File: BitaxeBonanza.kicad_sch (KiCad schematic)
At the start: 10 parts, among them J1 XT30

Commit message: most placement and routing done
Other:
- sheet Data ports: added 12V; removed none
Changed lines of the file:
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@@
+		(color 0 0 0 0)
+	)
+	(junction
+		(at 78.74 44.45)
+		(diameter 0)
 		(color 0 0 0 0)
 	)
@@
 	(wire
 		(pts
-			(xy 58.42 44.45) (xy 102.87 44.45)
+			(xy 58.42 44.45) (xy 78.74 44.45)
 		)
 		(stroke
@@
 	(wire
 		(pts
-			(xy 90.17 125.73) (xy 102.87 125.73)
+			(xy 90.17 129.54) (xy 102.87 129.54)
 		)
 		(stroke
@@
 	(wire
 		(pts
+			(xy 102.87 124.46) (xy 78.74 124.46)
+		)
+		(stroke
+			(width 0)
+			(type default)
+		)
+	)
+	(wire
+		(pts
 			(xy 58.42 48.26) (xy 62.23 48.26)
 		)
@@
 	(wire
 		(pts
+			(xy 78.74 44.45) (xy 102.87 44.45)
+		)
+		(stroke
+			(width 0)
+			(type default)
+		)
+	)
+	(wire
+		(pts
 			(xy 86.36 116.84) (xy 102.87 116.84)
 		)
@@
 		(pts
 			(xy 91.44 66.04) (xy 102.87 66.04)
+		)
+		(stroke
+			(width 0)
+			(type default)
+		)
+	)
+	(wire
+		(pts
+			(xy 78.74 124.46) (xy 78.74 44.45)
 		)
 		(stroke
@@
 	)
 	(label "5V_SWITCH"
-		(at 90.17 125.73 0)
+		(at 90.17 129.54 0)
 		(effects
 			(font
@@
 		)
 		(pin "5V_SWITCH" output
-			(at 102.87 125.73 180)
+			(at 102.87 129.54 180)
 			(effects
 				(font
@@
 			)
 		)
+		(pin "12V" input
+			(at 102.87 124.46 180)
+			(effects
+				(font
+					(size 1.27 1.27)
+				)
+				(justify left)
+			)
+		)

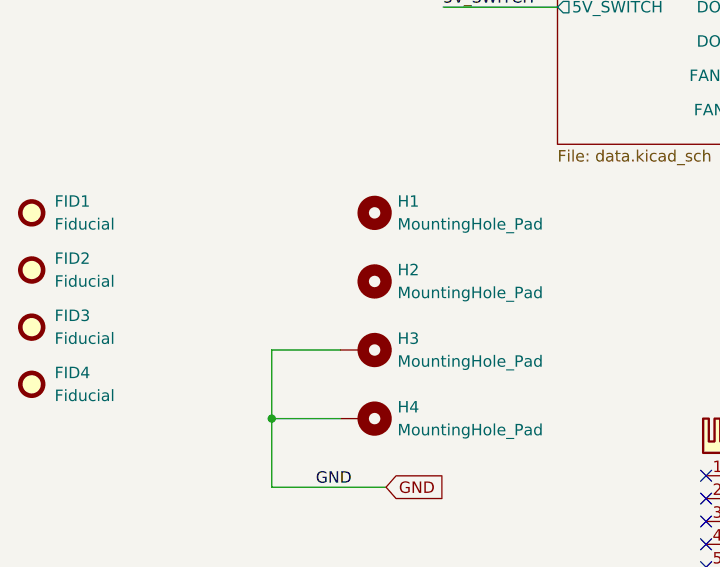
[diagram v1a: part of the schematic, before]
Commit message: changed TPS82130 voltage regulators to TPSM82903. Connected ESP32<->RP2040 CTRL serial port. made top mounting holes plated.
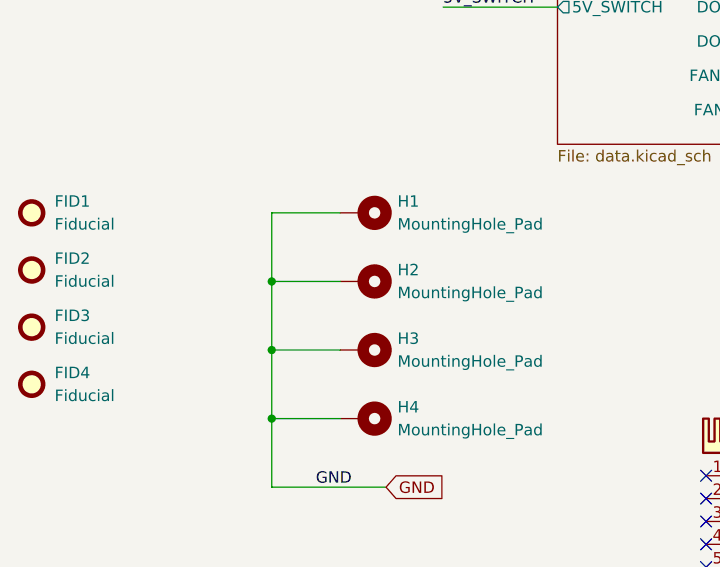
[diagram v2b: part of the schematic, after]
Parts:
- H1, H2: footprint MountingHole:MountingHole_3.2mm_M3 -> MountingHole:MountingHole_3.2mm_M3_Pad_Via; symbol Mechanical:MountingHole -> Mechanical:MountingHole_Pad
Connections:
- net GND: now also H1.1, H2.1
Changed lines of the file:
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@@
+	)
+	(junction
+		(at 71.12 160.02)
+		(diameter 0)
+		(color 0 0 0 0)
 	)
 	(junction
@@
 		(color 0 0 0 0)
 	)
+	(junction
+		(at 71.12 167.64)
+		(diameter 0)
+		(color 0 0 0 0)
+	)
 	(no_connect
 		(at 119.38 189.23)
@@
 	(wire
 		(pts
+			(xy 71.12 160.02) (xy 78.74 160.02)
+		)
+		(stroke
+			(width 0)
+			(type default)
+		)
+	)
+	(wire
+		(pts
 			(xy 153.67 116.84) (xy 128.27 116.84)
 		)
@@
 	(wire
 		(pts
+			(xy 78.74 152.4) (xy 71.12 152.4)
+		)
+		(stroke
+			(width 0)
+			(type default)
+		)
+	)
+	(wire
+		(pts
 			(xy 151.13 57.15) (xy 151.13 113.03)
 		)
@@
 	(wire
 		(pts
+			(xy 71.12 152.4) (xy 71.12 160.02)
+		)
+		(stroke
+			(width 0)
+			(type default)
+		)
+	)
+	(wire
+		(pts
 			(xy 148.59 53.34) (xy 148.59 109.22)
 		)
@@
 		(pts
 			(xy 128.27 140.97) (xy 198.12 140.97)
+		)
+		(stroke
+			(width 0)
+			(type default)
+		)
+	)
+	(wire
+		(pts
+			(xy 71.12 160.02) (xy 71.12 167.64)
 		)
 		(stroke
@@
 	)
 	(symbol
-		(lib_id "Mechanical:MountingHole")
-		(at 82.55 160.02 270)
+		(lib_id "Mechanical:MountingHole_Pad")
+		(at 81.28 160.02 270)
 		(unit 1)
 		(exclude_from_sim no)
@@
 			)
 		)
-		(property "Footprint" "MountingHole:MountingHole_3.2mm_M3"
-			(at 82.55 160.02 0)
+		(property "Footprint" "MountingHole:MountingHole_3.2mm_M3_Pad_Via"
+			(at 81.28 160.02 0)
 			(effects
 				(font
@@
 		)
 		(property "Datasheet" "~"
-			(at 82.55 160.02 0)
-			(effects
-				(font
-					(size 1.27 1.27)
-				)
-				(hide yes)
-			)
-		)
-		(property "Description" "Mounting Hole without connection"
-			(at 82.55 160.02 0)
+			(at 81.28 160.02 0)
+			(effects
+				(font
+					(size 1.27 1.27)
+				)
+				(hide yes)
+			)
+		)
+		(property "Description" "Mounting Hole with connection"
+			(at 81.28 160.02 0)
 			(effects
 				(font
@@
 		)
 		(property "Mouser" ""
-			(at 82.55 160.02 90)
+			(at 81.28 160.02 90)
 			(effects
 				(font
@@
 		)
 		(property "Manufacturer" ""
-			(at 82.55 160.02 90)
-			(effects
-				(font
-					(size 1.27 1.27)
-				)
-				(hide yes)
-			)
+			(at 81.28 160.02 90)
+			(effects
+				(font
+					(size 1.27 1.27)
+				)
+				(hide yes)
+			)
+		)
+		(pin "1"
 		)
 		(instances
@@
 	)
 	(symbol
-		(lib_id "Mechanical:MountingHole")
-		(at 82.55 152.4 270)
+		(lib_id "Mechanical:MountingHole_Pad")
+		(at 81.28 152.4 270)
 		(unit 1)
 		(exclude_from_sim no)
@@
 			)
 		)
-		(property "Footprint" "MountingHole:MountingHole_3.2mm_M3"
-			(at 82.55 152.4 0)
+		(property "Footprint" "MountingHole:MountingHole_3.2mm_M3_Pad_Via"
+			(at 81.28 152.4 0)
 			(effects
 				(font
@@
 		)
 		(property "Datasheet" "~"
-			(at 82.55 152.4 0)
-			(effects
-				(font
-					(size 1.27 1.27)
-				)
-				(hide yes)
-			)
-		)
-		(property "Description" "Mounting Hole without connection"
-			(at 82.55 152.4 0)
+			(at 81.28 152.4 0)
+			(effects
+				(font
+					(size 1.27 1.27)
+				)
+				(hide yes)
+			)
+		)
+		(property "Description" "Mounting Hole with connection"
+			(at 81.28 152.4 0)
 			(effects
 				(font
@@
 		)
 		(property "Mouser" ""
-			(at 82.55 152.4 90)
+			(at 81.28 152.4 90)
 			(effects
 				(font
@@
 		)
 		(property "Manufacturer" ""
-			(at 82.55 152.4 90)
-			(effects
-				(font
-					(size 1.27 1.27)
-				)
-				(hide yes)
-			)
+			(at 81.28 152.4 90)
+			(effects
+				(font
+					(size 1.27 1.27)
+				)
+				(hide yes)
+			)
+		)
+		(pin "1"
 		)
 		(instances

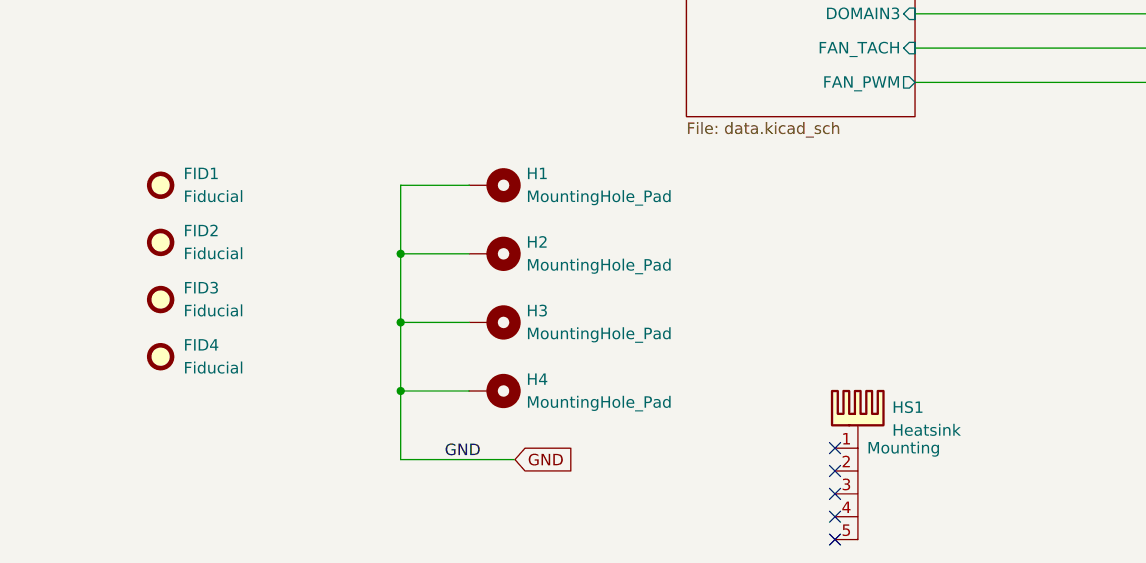
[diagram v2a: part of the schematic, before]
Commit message: switched to SMD FFC for the display connector
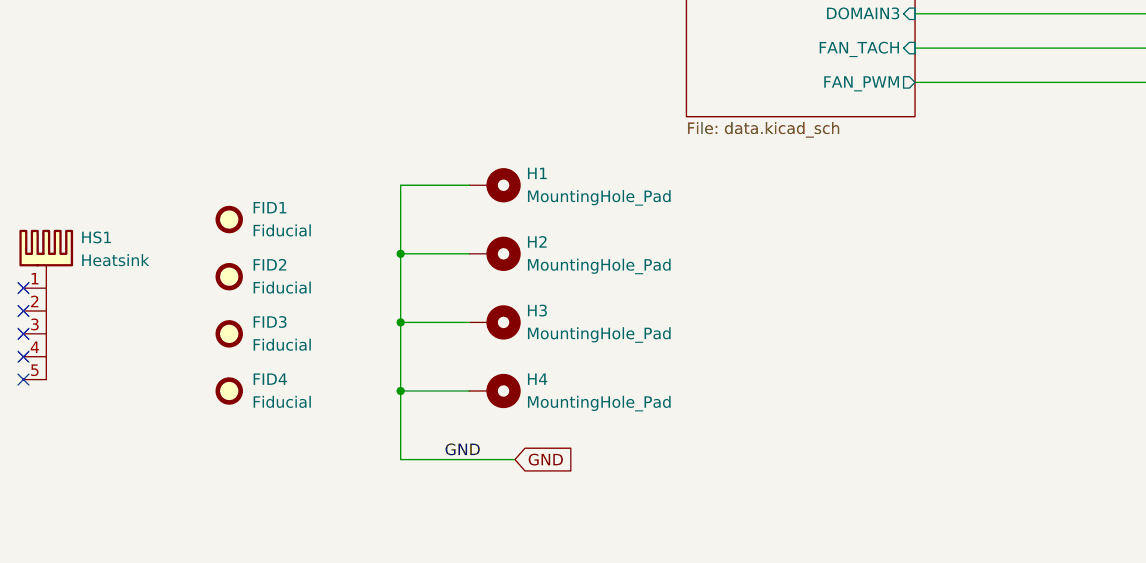
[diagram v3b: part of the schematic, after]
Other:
- moved on the sheet: FID1, FID2, FID3, FID4
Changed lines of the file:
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@@
 	)
 	(no_connect
-		(at 119.38 189.23)
+		(at 29.21 171.45)
 	)
 	(no_connect
-		(at 119.38 186.69)
+		(at 29.21 168.91)
 	)
 	(no_connect
-		(at 119.38 191.77)
+		(at 29.21 173.99)
 	)
 	(no_connect
-		(at 119.38 181.61)
+		(at 29.21 163.83)
 	)
 	(no_connect
-		(at 119.38 184.15)
+		(at 29.21 166.37)
 	)
 	(wire
@@
 	(symbol
 		(lib_id "bitaxe:Heatsink")
-		(at 121.92 179.07 0)
+		(at 31.75 161.29 0)
 		(unit 1)
 		(exclude_from_sim yes)
@@
 		(on_board yes)
 		(dnp no)
-		(fields_autoplaced yes)
 		(property "Reference" "HS1"
-			(at 125.73 177.1014 0)
+			(at 35.56 158.242 0)
 			(effects
 				(font
@@
 		)
 		(property "Value" "Heatsink"
-			(at 125.73 179.6414 0)
+			(at 35.56 160.782 0)
 			(effects
 				(font
@@
 		)
 		(property "Footprint" "bitaxe:Heatsink-5hole-BitaxeGT"
-			(at 122.2248 179.07 0)
+			(at 32.0548 161.29 0)
 			(effects
 				(font
@@
 		)
 		(property "Datasheet" "~"
-			(at 122.2248 179.07 0)
+			(at 32.0548 161.29 0)
 			(effects
 				(font
@@
 		)
 		(property "Description" "Heatsink"
-			(at 121.92 179.07 0)
+			(at 31.75 161.29 0)
 			(effects
 				(font
@@
 		)
 		(property "Mouser" ""
-			(at 121.92 179.07 0)
+			(at 31.75 161.29 0)
 			(effects
 				(font
@@
 		)
 		(property "Manufacturer" ""
-			(at 121.92 179.07 0)
+			(at 31.75 161.29 0)
 			(effects
 				(font
@@
 	(symbol
 		(lib_id "Mechanical:Fiducial")
-		(at 44.45 158.75 0)
+		(at 52.07 162.56 0)
 		(unit 1)
 		(exclude_from_sim yes)
@@
 		(fields_autoplaced yes)
 		(property "Reference" "FID2"
-			(at 46.99 157.4799 0)
+			(at 54.61 161.2899 0)
 			(effects
 				(font
@@
 		)
 		(property "Value" "Fiducial"
-			(at 46.99 160.0199 0)
+			(at 54.61 163.8299 0)
 			(effects
 				(font
@@
 		)
 		(property "Footprint" "bitaxe:Fiducial_1mm_Mask2mm"
-			(at 44.45 158.75 0)
+			(at 52.07 162.56 0)
 			(effects
 				(font
@@
 		)
 		(property "Datasheet" "~"
-			(at 44.45 158.75 0)
+			(at 52.07 162.56 0)
 			(effects
 				(font
@@
 		)
 		(property "Description" "Fiducial Marker"
-			(at 44.45 158.75 0)
+			(at 52.07 162.56 0)
 			(effects
 				(font
@@
 		)
 		(property "Mouser" ""
-			(at 44.45 158.75 0)
+			(at 52.07 162.56 0)
 			(effects
 				(font
@@
 		)
 		(property "Manufacturer" ""
-			(at 44.45 158.75 0)
+			(at 52.07 162.56 0)
 			(effects
 				(font
@@
 	(symbol
 		(lib_id "Mechanical:Fiducial")
-		(at 44.45 171.45 0)
+		(at 52.07 175.26 0)
 		(unit 1)
 		(exclude_from_sim yes)
@@
 		(fields_autoplaced yes)
 		(property "Reference" "FID4"
-			(at 46.99 170.1799 0)
+			(at 54.61 173.9899 0)
 			(effects
 				(font
@@
 		)
 		(property "Value" "Fiducial"
-			(at 46.99 172.7199 0)
+			(at 54.61 176.5299 0)
 			(effects
 				(font
@@
 		)
 		(property "Footprint" "bitaxe:Fiducial_1mm_Mask2mm"
-			(at 44.45 171.45 0)
+			(at 52.07 175.26 0)
 			(effects
 				(font
@@
 		)
 		(property "Datasheet" "~"
-			(at 44.45 171.45 0)
+			(at 52.07 175.26 0)
 			(effects
 				(font
@@
 		)
 		(property "Description" "Fiducial Marker"
-			(at 44.45 171.45 0)
+			(at 52.07 175.26 0)
 			(effects
 				(font
@@
 		)
 		(property "Mouser" ""
-			(at 44.45 171.45 0)
+			(at 52.07 175.26 0)
 			(effects
 				(font
@@
 		)
 		(property "Manufacturer" ""
-			(at 44.45 171.45 0)
+			(at 52.07 175.26 0)
 			(effects
 				(font
@@
 	(symbol
 		(lib_id "Mechanical:Fiducial")
-		(at 44.45 152.4 0)
+		(at 52.07 156.21 0)
 		(unit 1)
 		(exclude_from_sim yes)
@@
 		(fields_autoplaced yes)
 		(property "Reference" "FID1"
-			(at 46.99 151.1299 0)
+			(at 54.61 154.9399 0)
 			(effects
 				(font
@@
 		)
 		(property "Value" "Fiducial"
-			(at 46.99 153.6699 0)
+			(at 54.61 157.4799 0)
 			(effects
 				(font
@@
 		)
 		(property "Footprint" "bitaxe:Fiducial_1mm_Mask2mm"
-			(at 44.45 152.4 0)
+			(at 52.07 156.21 0)
 			(effects
 				(font
@@
 		)
 		(property "Datasheet" "~"
-			(at 44.45 152.4 0)
+			(at 52.07 156.21 0)
 			(effects
 				(font
@@
 		)
 		(property "Description" "Fiducial Marker"
-			(at 44.45 152.4 0)
+			(at 52.07 156.21 0)
 			(effects
 				(font
@@
 		)
 		(property "Mouser" ""
-			(at 44.45 152.4 0)
+			(at 52.07 156.21 0)
 			(effects
 				(font
@@
 		)
 		(property "Manufacturer" ""
-			(at 44.45 152.4 0)
+			(at 52.07 156.21 0)
 			(effects
 				(font
@@
 	(symbol
 		(lib_id "Mechanical:Fiducial")
-		(at 44.45 165.1 0)
+		(at 52.07 168.91 0)
 		(unit 1)
 		(exclude_from_sim yes)
@@
 		(fields_autoplaced yes)
 		(property "Reference" "FID3"
-			(at 46.99 163.8299 0)
+			(at 54.61 167.6399 0)
 			(effects
 				(font
@@
 		)
 		(property "Value" "Fiducial"
-			(at 46.99 166.3699 0)
+			(at 54.61 170.1799 0)
 			(effects
 				(font
@@
 		)
 		(property "Footprint" "bitaxe:Fiducial_1mm_Mask2mm"
-			(at 44.45 165.1 0)
+			(at 52.07 168.91 0)
 			(effects
 				(font
@@
 		)
 		(property "Datasheet" "~"
-			(at 44.45 165.1 0)
+			(at 52.07 168.91 0)
 			(effects
 				(font
@@
 		)
 		(property "Description" "Fiducial Marker"
-			(at 44.45 165.1 0)
+			(at 52.07 168.91 0)
 			(effects
 				(font
@@
 		)
 		(property "Mouser" ""
-			(at 44.45 165.1 0)
+			(at 52.07 168.91 0)
 			(effects
 				(font
@@
 		)
 		(property "Manufacturer" ""
-			(at 44.45 165.1 0)
-			(effects
-				(font
+			(at 52.07 168.91 0)
+			(effects
+				(font

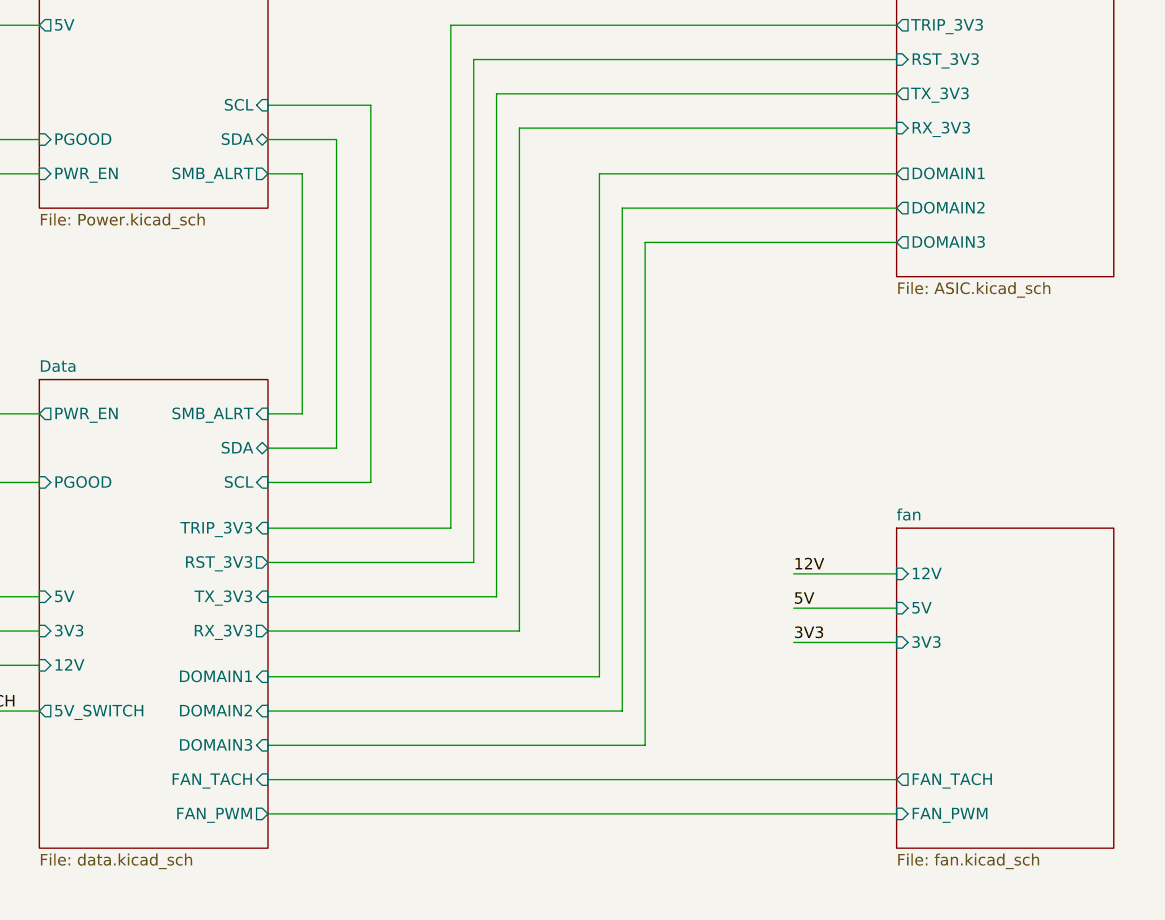
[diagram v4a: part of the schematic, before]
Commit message: part silkscreen cleanup
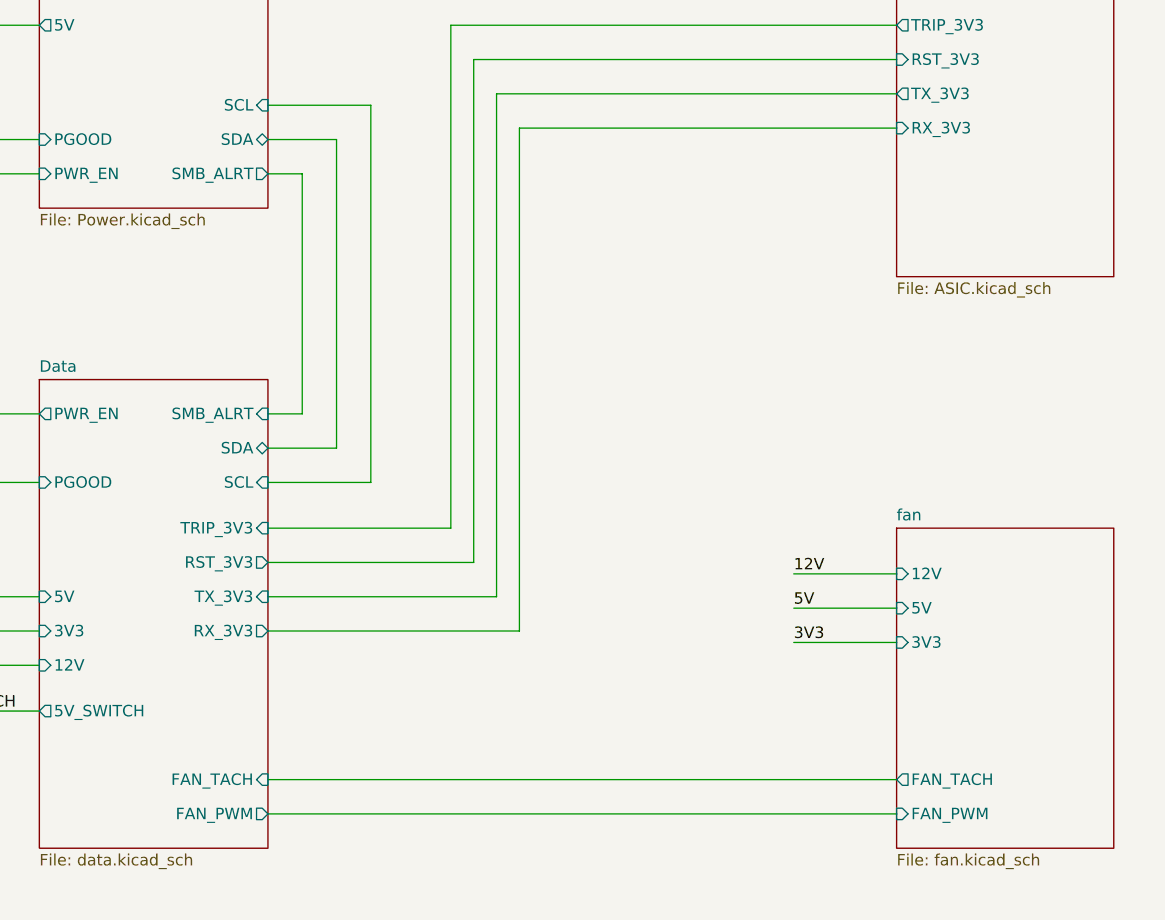
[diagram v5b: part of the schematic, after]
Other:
- sheet ASIC ports: added none; removed DOMAIN1, DOMAIN2, DOMAIN3
- sheet Data ports: added none; removed DOMAIN1, DOMAIN2, DOMAIN3
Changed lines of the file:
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@@
-	(wire
-		(pts
-			(xy 128.27 129.54) (xy 167.64 129.54)
-		)
-		(stroke
-			(width 0)
-			(type default)
-		)
-	)
-	(wire
-		(pts
-			(xy 165.1 69.85) (xy 165.1 125.73)
-		)
-		(stroke
-			(width 0)
-			(type default)
-		)
-	)
-	(wire
-		(pts
-			(xy 167.64 129.54) (xy 167.64 73.66)
-		)
-		(stroke
-			(width 0)
-			(type default)
-		)
-	)
 	(wire
 		(pts
@@
 	(wire
 		(pts
-			(xy 198.12 77.47) (xy 170.18 77.47)
-		)
-		(stroke
-			(width 0)
-			(type default)
-		)
-	)
-	(wire
-		(pts
 			(xy 102.87 53.34) (xy 86.36 53.34)
 		)
@@
 	(wire
 		(pts
-			(xy 165.1 125.73) (xy 128.27 125.73)
-		)
-		(stroke
-			(width 0)
-			(type default)
-		)
-	)
-	(wire
-		(pts
 			(xy 96.52 96.52) (xy 102.87 96.52)
 		)
@@
 	(wire
 		(pts
-			(xy 170.18 77.47) (xy 170.18 133.35)
-		)
-		(stroke
-			(width 0)
-			(type default)
-		)
-	)
-	(wire
-		(pts
 			(xy 71.12 167.64) (xy 71.12 175.26)
 		)
@@
 	(wire
 		(pts
-			(xy 198.12 69.85) (xy 165.1 69.85)
-		)
-		(stroke
-			(width 0)
-			(type default)
-		)
-	)
-	(wire
-		(pts
 			(xy 78.74 44.45) (xy 102.87 44.45)
 		)
@@
 	(wire
 		(pts
-			(xy 170.18 133.35) (xy 128.27 133.35)
-		)
-		(stroke
-			(width 0)
-			(type default)
-		)
-	)
-	(wire
-		(pts
 			(xy 91.44 66.04) (xy 102.87 66.04)
 		)
@@
 		(pts
 			(xy 78.74 124.46) (xy 78.74 44.45)
-		)
-		(stroke
-			(width 0)
-			(type default)
-		)
-	)
-	(wire
-		(pts
-			(xy 167.64 73.66) (xy 198.12 73.66)
 		)
 		(stroke
@@
 			)
 		)
-		(pin "DOMAIN1" input
-			(at 128.27 125.73 0)
-			(effects
-				(font
-					(size 1.27 1.27)
-				)
-				(justify right)
-			)
-		)
-		(pin "DOMAIN2" input
-			(at 128.27 129.54 0)
-			(effects
-				(font
-					(size 1.27 1.27)
-				)
-				(justify right)
-			)
-		)
-		(pin "DOMAIN3" input
-			(at 128.27 133.35 0)
-			(effects
-				(font
-					(size 1.27 1.27)
-				)
-				(justify right)
-			)
-		)
 		(pin "FAN_PWM" output
 			(at 128.27 140.97 0)
@@
 			(effects
 				(font
-					(size 1.27 1.27)
-				)
-				(justify left)
-			)
-		)
-		(pin "DOMAIN1" output
-			(at 198.12 69.85 180)
-			(effects
-				(font
-					(size 1.27 1.27)
-				)
-				(justify left)
-			)
-		)
-		(pin "DOMAIN2" output
-			(at 198.12 73.66 180)
-			(effects
-				(font
-					(size 1.27 1.27)
-				)
-				(justify left)
-			)
-		)
-		(pin "DOMAIN3" output
-			(at 198.12 77.47 180)
-			(effects
-				(font
